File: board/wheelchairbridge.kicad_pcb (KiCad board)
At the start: 2 copper layers, 53 parts, among them J1 male-joystick in, J10 grove-I2C-2, J2 female-to wheelchair, J3 12V, J4 AlarmIn1, J5 AlarmIn2, J6 grove-Serial, J7 grove-I2C, J8 grove-I2C-2, J9 grove-I2C, K1 RTE2xxxx, M1 Module_RaspberryPi_PicoW_Sock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, Q2 BC850, U1 LM7805_TO220, U2 AD5282, U3 TIL111, U4 TIL111

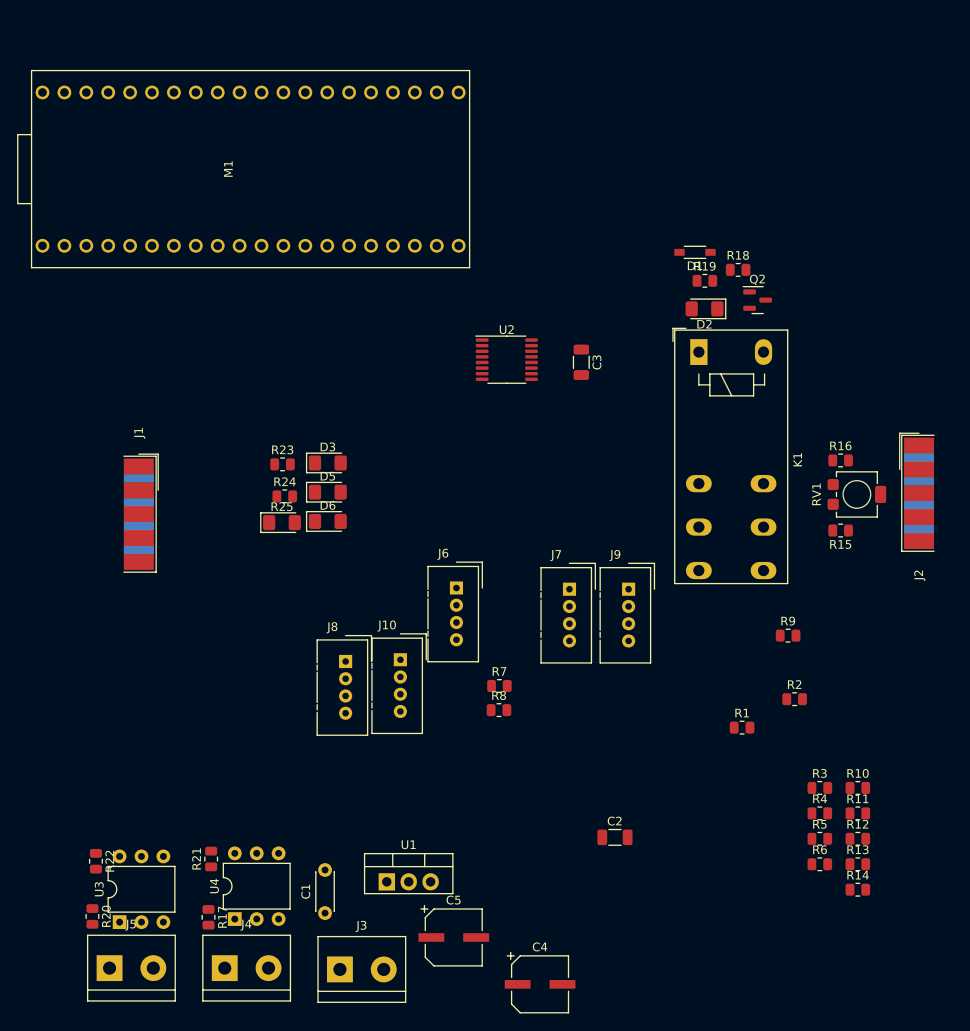
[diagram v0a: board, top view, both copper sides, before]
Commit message: Added Solid State relays for low-power signal switching. Switch from edge to regular DB9 connectors Refactored schematic PCB layout
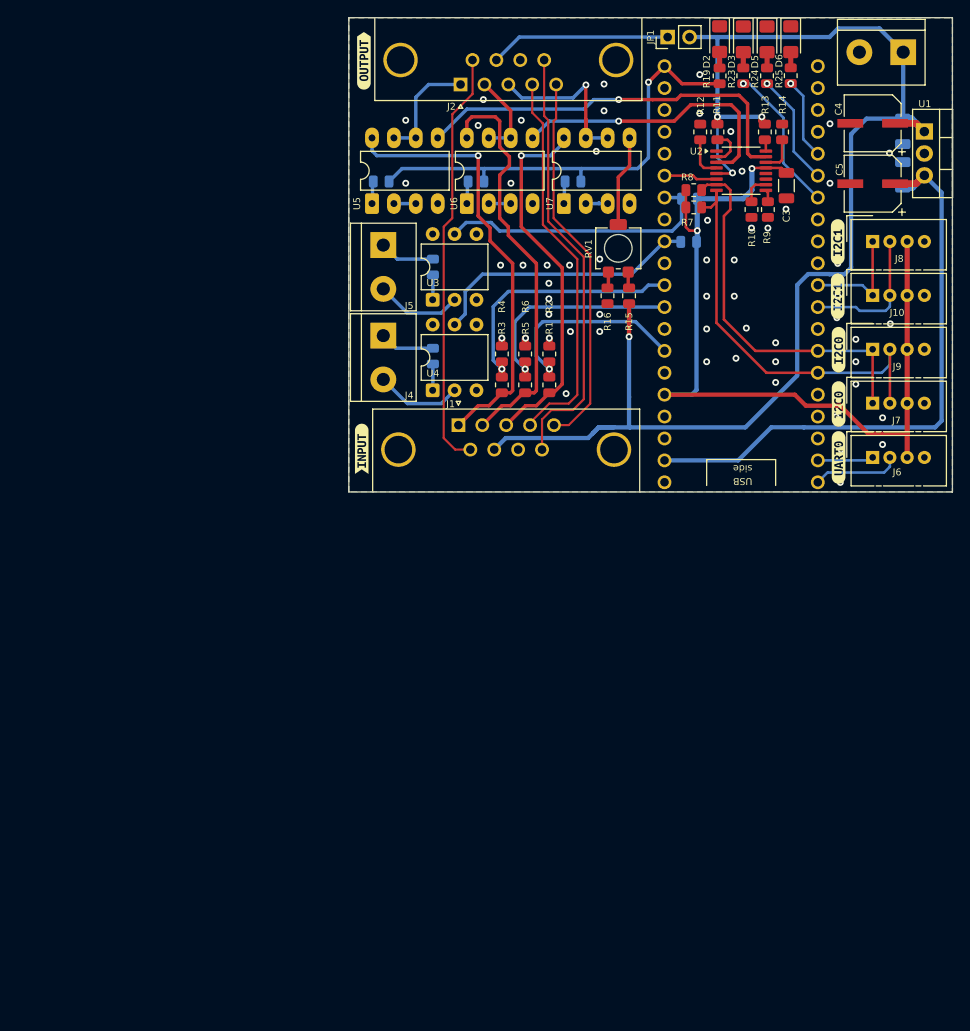
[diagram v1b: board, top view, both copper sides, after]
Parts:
- removed D1: Diode_Schottky_SOD123, fab:SOD-123
- removed K1: RTE2xxxx, Relay_THT:Relay_DPDT_Schrack-RT2-FormC_RM5mm
- removed Q2: BC850, Package_TO_SOT_SMD:SOT-23
- removed R18: 1k, Resistor_SMD:R_0805_2012Metric
- added JP1: power, Connector_PinHeader_2.54mm:PinHeader_1x02_P2.54mm_Vertical, F.Cu at (87.0, 52.2)
- added R26: 1k, Resistor_SMD:R_0805_2012Metric, B.Cu at (53.8, 69.0)
- added R27: 1k, Resistor_SMD:R_0805_2012Metric, B.Cu at (64.8, 69.0)
- added R28: 1k, Resistor_SMD:R_0805_2012Metric, B.Cu at (76.0, 69.0)
- added U5: LH1512BB, Package_DIP:DIP-8_W7.62mm_Socket_LongPads, F.Cu at (52.7, 71.6)
- added U6: LH1512BB, Package_DIP:DIP-8_W7.62mm_Socket_LongPads, F.Cu at (63.7, 71.6)
- added U7: LH1512BB, Package_DIP:DIP-8_W7.62mm_Socket_LongPads, F.Cu at (74.9, 71.6)
- added kibuzzard-681B47BC: G***, kibuzzard-681B47BC, F.Cu at (51.8, 55.0)
- added kibuzzard-681B47CA: G***, kibuzzard-681B47CA, F.Cu at (51.5, 100.0)
- added kibuzzard-681B47D9: G***, kibuzzard-681B47D9, B.Cu at (56.9, 78.9)
- added kibuzzard-681B4932: G***, kibuzzard-681B4932, B.Cu at (111.8, 57.3)
- added kibuzzard-681B49F5: G***, kibuzzard-681B49F5, B.Cu at (56.9, 89.5)
- added kibuzzard-681B4A1A: G***, kibuzzard-681B4A1A, F.Cu at (106.7, 76.0)
- added kibuzzard-681B4A1A: G***, kibuzzard-681B4A1A, F.Cu at (106.7, 82.3)
- added kibuzzard-681B4A2D: G***, kibuzzard-681B4A2D, F.Cu at (106.8, 88.5)
- added kibuzzard-681B4A2D: G***, kibuzzard-681B4A2D, F.Cu at (106.8, 94.8)
- added kibuzzard-681B4A44: G***, kibuzzard-681B4A44, F.Cu at (106.8, 101.0)
- C1: footprint Capacitor_THT:C_Disc_D4.3mm_W1.9mm_P5.00mm -> Capacitor_SMD:C_1206_3216Metric; moved to B.Cu
- C2, R17, R20, R21, R22: moved to B.Cu
- J1: footprint Connector_Dsub:DSUB-9_Male_EdgeMount_P2.77mm -> Connector_Dsub:DSUB-9_Pins_Horizontal_P2.77x2.84mm_EdgePinOffset4.94mm_Housed_MountingHolesOffset4.94mm
- J2: footprint Connector_Dsub:DSUB-9_Female_EdgeMount_P2.77mm -> Connector_Dsub:DSUB-9_Socket_Horizontal_P2.77x2.84mm_EdgePinOffset4.94mm_Housed_MountingHolesOffset4.94mm
- R25: footprint LED_SMD:LED_1206_3216Metric_Pad1.42x1.75mm_HandSolder -> Resistor_SMD:R_0805_2012Metric
- moved J3 124.8 mm to (114.3, 54.0), turned to 180 degrees
- moved C1 112.7 mm to (114.2, 63.2), turned to -90 degrees
- moved C4 107.0 mm to (110.8, 62.2), turned to 180 degrees
- moved U1 107.0 mm to (116.8, 63.2), turned to -90 degrees
- moved R22 103.1 mm to (89.5, 71.0), turned to 180 degrees
- moved C5 100.0 mm to (110.8, 69.2), turned to 180 degrees
- moved R21 90.5 mm to (89.4, 76.0), turned to 180 degrees
- moved J5 89.7 mm to (54.0, 76.4), turned to -90 degrees
- moved R14 88.3 mm to (100.2, 63.2), turned to 90 degrees
- moved R13 85.6 mm to (98.2, 63.2), turned to 90 degrees
- moved R20 85.0 mm to (59.8, 78.9), turned to 90 degrees
- moved R12 84.0 mm to (90.8, 63.2), turned to 90 degrees
- moved C2 83.8 mm to (114.2, 68.2), turned to 90 degrees
- moved U3 80.8 mm to (59.7, 82.7)
- moved R11 80.7 mm to (92.8, 63.2), turned to 90 degrees
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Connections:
- net Net-(J1-Pad1) renamed /VsrcX
- net Net-(J1-Pad2) renamed /VsrcY
- net Net-(J1-Pad3) renamed /VsrcCenter
- D2 pad 1: Net-(D2-K) -> GND
- D2 pad 2: +5V -> Net-(D2-A)
- D3 pad 1: Net-(D3-K) -> GND
- D3 pad 2: /LED-red -> Net-(D3-A)
- D5 pad 1: Net-(D5-K) -> GND
- D5 pad 2: /LED-green -> Net-(D5-A)
- D6 pad 1: Net-(D6-K) -> GND
- D6 pad 2: /LED_blue -> Net-(D6-A)
- J10 pad 1: /SDA2 -> /SCL1
- J2 pad 1: Net-(J2-Pad1) -> /VoutX
- J2 pad 2: Net-(J2-Pad2) -> /VoutY
- J2 pad 3: Net-(J2-Pad3) -> /VoutCenter
- J2 pad 7: +12V -> Net-(JP1-A)
- J8 pad 1: /SDA2 -> /SCL1
- M1 pad 14: unconnected-(M1-GP10-Pad14) -> /LED-red
- M1 pad 15: unconnected-(M1-GP11-Pad15) -> /LED-green
- M1 pad 16: unconnected-(M1-GP12-Pad16) -> /LED-blue
- M1 pad 17: /LED-red -> unconnected-(M1-GP13-Pad17)
- M1 pad 19: /LED-green -> unconnected-(M1-GP14-Pad19)
- M1 pad 20: /LED-blue -> unconnected-(M1-GP15-Pad20)
- M1 pad 22: /SHDN -> unconnected-(M1-GP17-Pad22)
- M1 pad 26: unconnected-(M1-GP20-Pad26) -> /SHDN
- M1 pad 31: /VjoyCenter -> /VjoyX
- M1 pad 34: /VjoyX -> /VjoyCenter
- R19 pad 1: Net-(D1-A) -> Net-(D2-A)
- R19 pad 2: Net-(D2-K) -> /enable
- R23 pad 1: GND -> /LED-red
- R23 pad 2: Net-(D3-K) -> Net-(D3-A)
- R24 pad 1: GND -> /LED-green
- R24 pad 2: Net-(D5-K) -> Net-(D5-A)
- R25 pad 1: GND -> /LED-blue
- R25 pad 2: Net-(D6-K) -> Net-(D6-A)
- RV1 pad 2: Net-(J2-Pad3) -> /VctlCenter
- U2 pad 15: Net-(U2-W2) -> /VctlX
- U2 pad 3: unconnected-(U2-W1-Pad3) -> /VctlY
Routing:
- net +12V: track 0.00 -> 162.0 mm, vias 0 -> 4
- net +3.3V: track 0.00 -> 100.5 mm, vias 0 -> 2
- net +5V: track 0.00 -> 70.2 mm
- net /enable: track 0.00 -> 52.9 mm, vias 0 -> 1
- net /VsrcX: track 0.00 -> 50.9 mm, vias 0 -> 1
- net /db-9: track 0.00 -> 50.6 mm
- net /SDA: track 0.00 -> 49.6 mm
- net /db-6: track 0.00 -> 48.9 mm
- net /VsrcY: track 0.00 -> 48.0 mm
- net /VctlX: track 0.00 -> 46.4 mm, vias 0 -> 1
- net /db-4: track 0.00 -> 45.3 mm
- net /SCL: track 0.00 -> 44.2 mm
- net /db-5: track 0.00 -> 44.1 mm
- net /VsrcCenter: track 0.00 -> 43.0 mm, vias 0 -> 1
- net /VctlY: track 0.00 -> 33.8 mm, vias 0 -> 1
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- added copper zone on B.Cu, net GND
- added copper zone on F.Cu, net GND
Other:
- board outline added: 70 x 55 mm

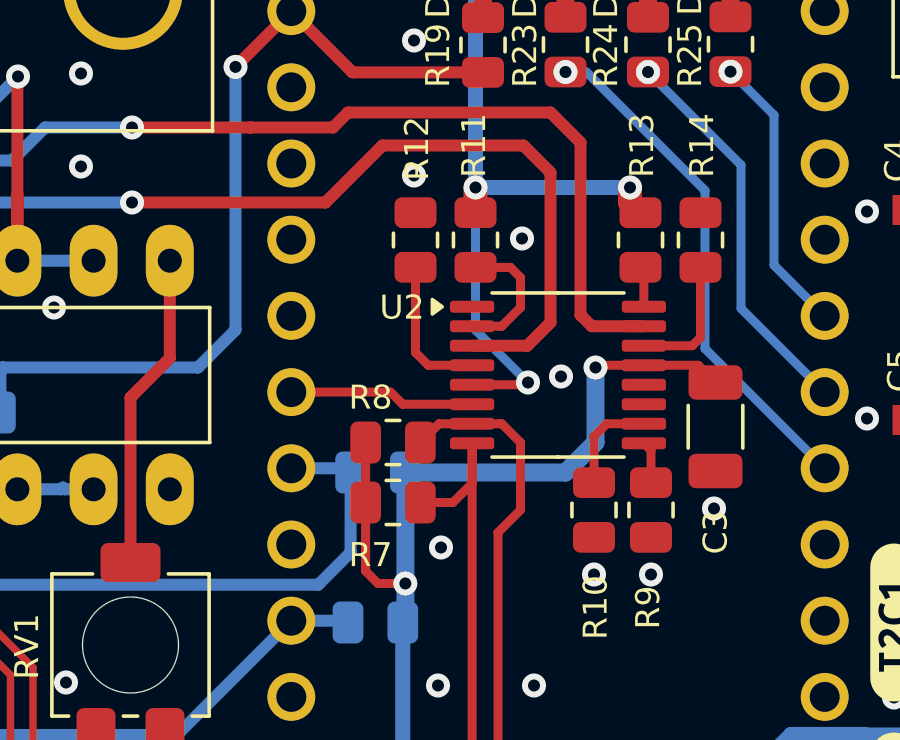
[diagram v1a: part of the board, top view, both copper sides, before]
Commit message: Alarm labels were wrong Added 100nF cap on 12V for digipot
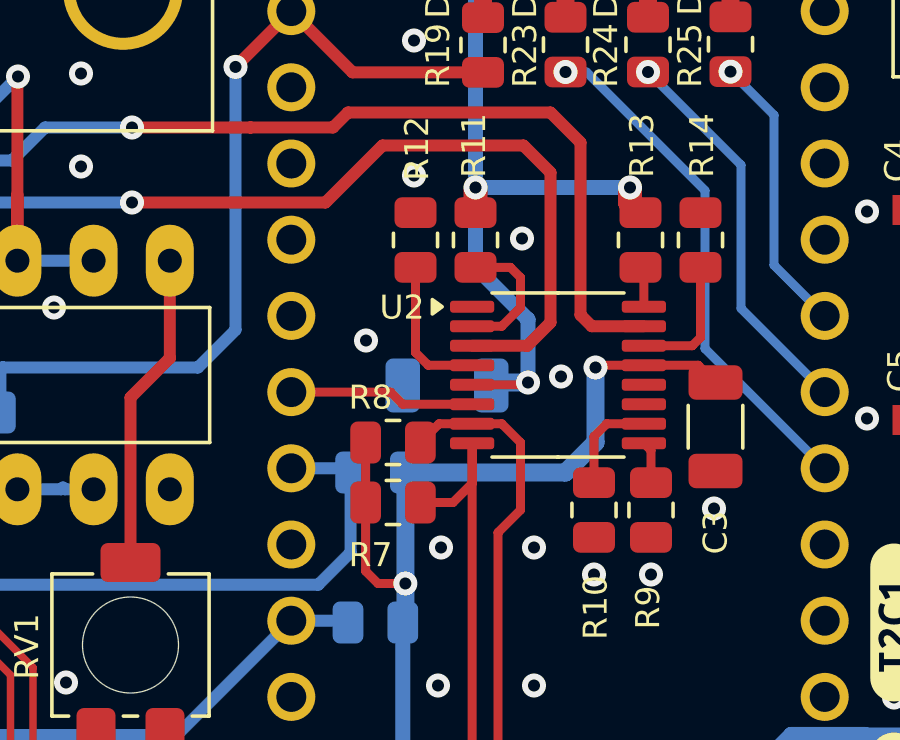
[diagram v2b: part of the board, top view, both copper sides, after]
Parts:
- removed kibuzzard-681B47D9: G***, kibuzzard-681B47D9
- removed kibuzzard-681B49F5: G***, kibuzzard-681B49F5
- added C6: 100nF, Capacitor_SMD:C_1206_3216Metric, B.Cu at (91.8, 68.1)
- added kibuzzard-681C614D: G***, kibuzzard-681C614D, B.Cu at (56.9, 78.9)
- added kibuzzard-681C6150: G***, kibuzzard-681C6150, B.Cu at (56.9, 89.5)
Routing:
- net +12V: track 162.0 -> 163.2 mm
- net GND: vias 58 -> 60
